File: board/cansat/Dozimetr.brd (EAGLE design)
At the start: 31.5 x 94 mm, 47 parts, among them U1 LMC555CMX/NOPB

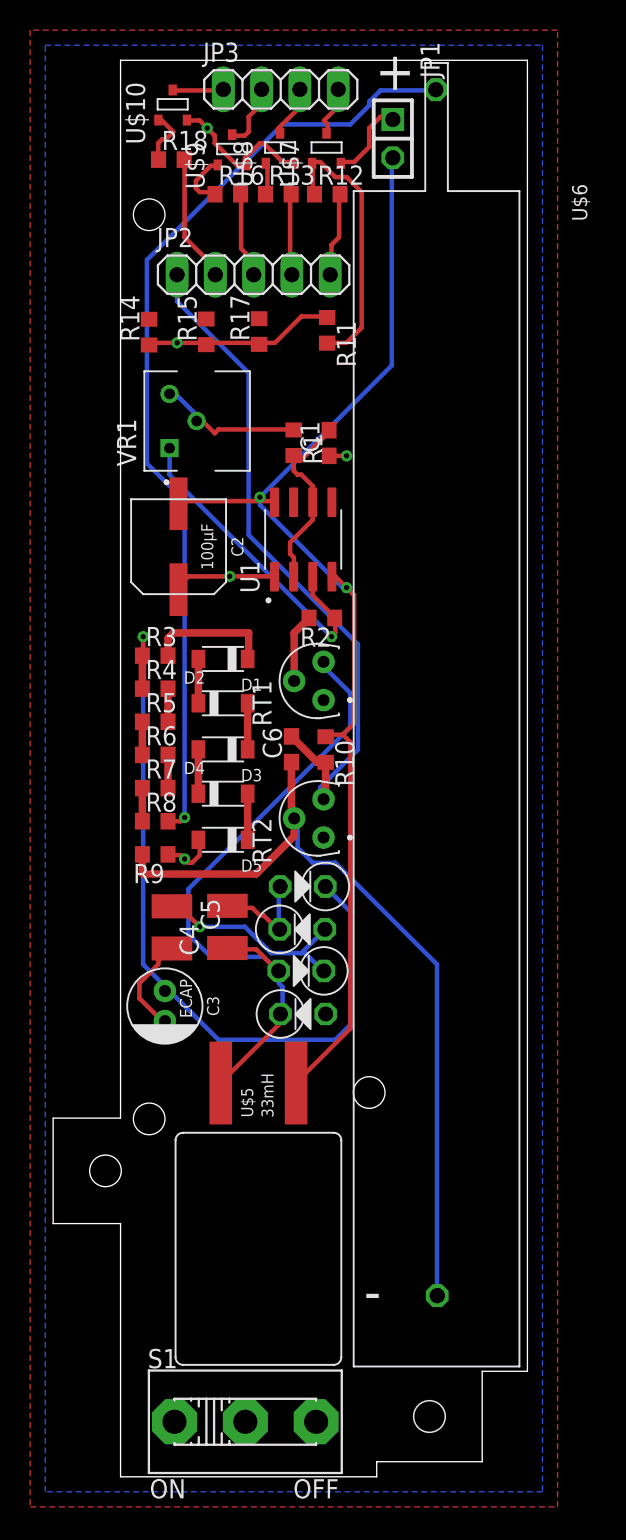
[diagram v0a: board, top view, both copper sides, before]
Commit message: Расставлены подписи на плате
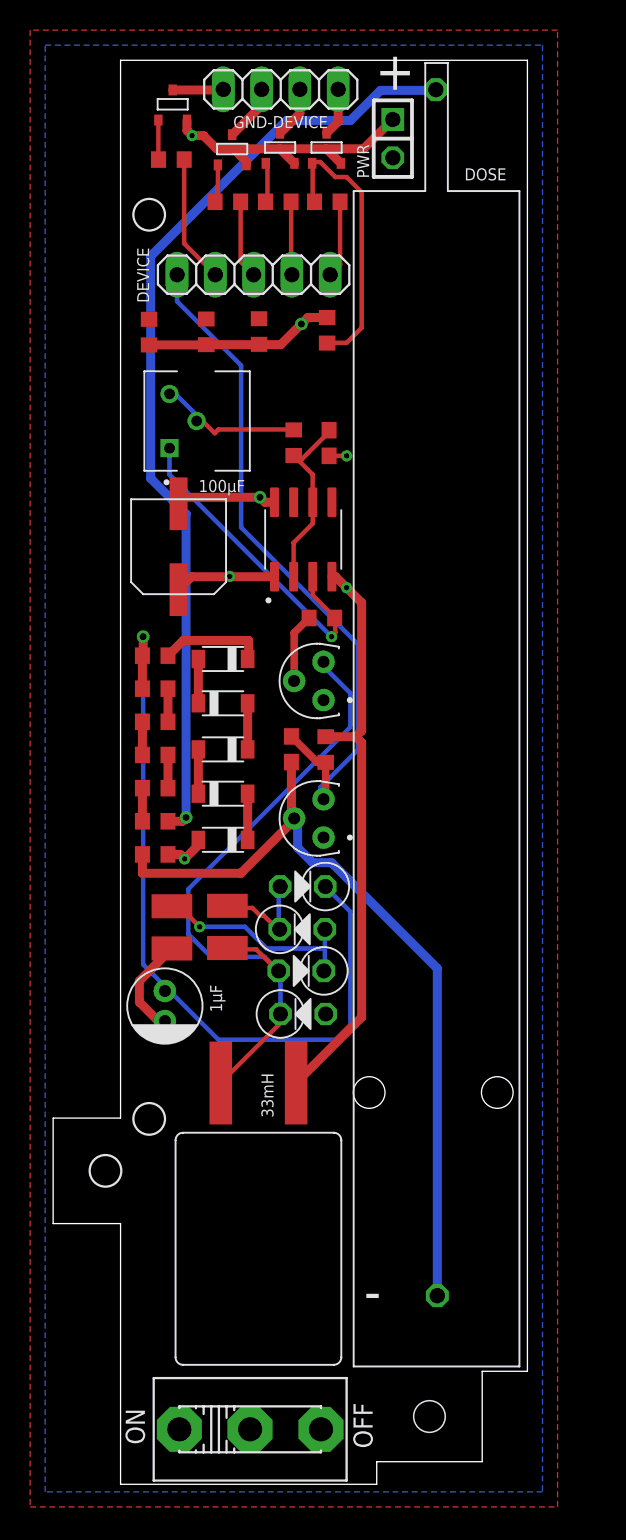
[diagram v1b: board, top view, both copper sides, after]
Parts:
- C3: value ECAP -> 1μF
- D1, D2, D3, D4, D5: value DIODE-MBR -> MBR
- U1: value LMC555CMX/NOPB -> LMC555
- VR1: value 3362H-1-502LF -> 3362H
- moved S1 0.59 mm to (8.60, -3.85)
- moved R12 0.50 mm to (13.7, 77.6)
- moved R13 0.50 mm to (10.5, 77.6)
- moved R16 0.50 mm to (7.12, 77.6)
- renumbered JP1 to PWR, JP2 to DEVICE, JP3 to GND-DEVICE, U$10 to SI2302-1, U$6 to DOSE, U$7 to SI2302-4, U$8 to SI2302-3, U$9 to SI2302-2
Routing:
- net 5V1: track 79.0 -> 45.4 mm
- net GND: track 46.9 -> 50.7 mm
- net N$13: track 8.41 -> 7.03 mm
- net N$28: track 3.88 -> 2.53 mm
- net N$25: track 3.71 -> 2.63 mm
- net N$19: track 53.9 -> 53.0 mm
- net GND-MOTOR: track 4.40 -> 3.82 mm
- net DVIG: track 5.39 -> 4.86 mm
- net N$31: track 18.0 -> 18.5 mm
- net N$30: track 2.14 -> 2.64 mm
- added copper zone on layer 1, net 5V1
- removed copper zone on layer 1, net 3V3
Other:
- board size 31.5 x 94 mm -> 31.5 x 94.5 mm
